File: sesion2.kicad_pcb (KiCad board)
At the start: 2 copper layers, 45 x 35.5 mm, 14 parts, among them IC1 AT89LS51-16AU, J1 1366004, J2 68000-106HLF

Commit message: Sesion4
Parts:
- removed PS1: TAR5SB30_TE85L,F_, Samacsys:SOT95P275X140-5N
- added C8: 100 nF, Capacitor_SMD:C_0402_1005Metric, F.Cu at (94.1, 100.0)
- added C9: 100nF, Capacitor_SMD:C_0402_1005Metric, F.Cu at (92.5, 122.0)
- added CCOMP1: 82 nF, Capacitor_SMD:C_0402_1005Metric, F.Cu at (82.5, 120.4)
- added CCOMP2: 180pF, Capacitor_SMD:C_0402_1005Metric, F.Cu at (77.4, 120.4)
- added Cboot1: 100 nF, Capacitor_SMD:C_0402_1005Metric, F.Cu at (81.5, 115.0)
- added Cin1: 4.7 uF, Capacitor_SMD:C_0402_1005Metric, F.Cu at (78.0, 110.5)
- added Cin2: 4.7 uF, Capacitor_SMD:C_0402_1005Metric, F.Cu at (80.0, 110.5)
- added Cout1: 22 uF, Capacitor_SMD:C_0402_1005Metric, F.Cu at (97.0, 111.0)
- added Cout2: 22 uF, Capacitor_SMD:C_0402_1005Metric, F.Cu at (95.0, 111.0)
- added D1: B560C, Samacsys:DIOM7959X250N, F.Cu at (90.5, 114.0)
- added IC2: VL53L1CXV0FY_1, Samacsys:VL53L1CXV0FY1, F.Cu at (97.3, 97.4)
- added IC3: MAX31855SASA+T, Samacsys:SOIC127P600X175-8N, F.Cu at (123.0, 100.0)
- added IC4: DS18B20Z+, Package_SO:SOIC-8_3.9x4.9mm_P1.27mm, F.Cu at (97.5, 128.0)
- added J3: Conn_01x05, Connector_PinHeader_2.54mm:PinHeader_1x05_P2.54mm_Vertical, F.Cu at (105.1, 135.0)
- added J4: Conn_01x02, TerminalBlock_Altech:Altech_AK100_1x02_P5.00mm, F.Cu at (126.0, 115.5)
- added J5: USB_C_Receptacle_USB2.0_16P, Connector_USB:USB_C_Receptacle_GCT_USB4105-xx-A_16P_TopMnt_Horizontal, F.Cu at (77.5, 131.5)
- added L1: 10uH, Inductor_SMD:L_1206_3216Metric, F.Cu at (96.0, 116.0)
- added R10: 5.1k, Resistor_SMD:R_0402_1005Metric_Pad0.72x0.64mm_HandSolder, F.Cu at (85.0, 134.5)
- added R4: 10k, Resistor_SMD:R_0402_1005Metric_Pad0.72x0.64mm_HandSolder, F.Cu at (110.5, 132.0)
- added R5: 4.7k, Resistor_SMD:R_0402_1005Metric_Pad0.72x0.64mm_HandSolder, F.Cu at (103.5, 124.5)
- added R6: 3.3k, Resistor_SMD:R_0402_1005Metric_Pad0.72x0.64mm_HandSolder, F.Cu at (103.0, 115.6)
- added R7: 3.3k, Resistor_SMD:R_0402_1005Metric_Pad0.72x0.64mm_HandSolder, F.Cu at (100.5, 96.0)
- added R8: 3.3k, Resistor_SMD:R_0402_1005Metric_Pad0.72x0.64mm_HandSolder, F.Cu at (110.0, 94.0)
- added R9: 5.1k, Resistor_SMD:R_0402_1005Metric_Pad0.72x0.64mm_HandSolder, F.Cu at (88.4, 134.5)
- added RCOMP1: 3.24, Resistor_SMD:R_0402_1005Metric_Pad0.72x0.64mm_HandSolder, F.Cu at (80.0, 120.4)
- added REN1: 100k, Resistor_SMD:R_0402_1005Metric_Pad0.72x0.64mm_HandSolder, F.Cu at (77.1, 106.5)
- added REN2: 10k, Resistor_SMD:R_0402_1005Metric_Pad0.72x0.64mm_HandSolder, F.Cu at (80.0, 106.5)
- added RFB1: 31.2k, Resistor_SMD:R_0402_1005Metric_Pad0.72x0.64mm_HandSolder, F.Cu at (74.4, 123.0)
- added RFB2: 10k, Resistor_SMD:R_0402_1005Metric_Pad0.72x0.64mm_HandSolder, F.Cu at (77.9, 123.0)
- added RRT1: 340k, Resistor_SMD:R_0402_1005Metric_Pad0.72x0.64mm_HandSolder, F.Cu at (74.0, 115.0)
- added U1: TPS54360BDDA, Samacsys:SOIC127P600X170-9N, F.Cu at (78.0, 115.0)
- added U2: CH340C, Package_SO:SOIC-16_3.9x9.9mm_P1.27mm, F.Cu at (88.0, 126.7)
- C1: value 1uF -> 100nF
- C2: value 0.01uF -> 100nF
- C3: value 10uF -> 100nF
- C5: value 100nF -> 10 nF
- C6: value 100nF -> 100 nF
- C7: value 100nF -> 4.7 nF
- IC1: value AT89LS51-16AU -> PIC16F18855-I_SP; footprint Samacsys:QFP80P1200X1200X120-44N -> Samacsys:DIP794W56P254L3486H508Q28N
- J1: value 1366004 -> TB0012-508-02GR; footprint Samacsys:1366004 -> Samacsys:TB0012-508-02GR
- J2: value 68000-106HLF -> Conn_01x05; footprint Samacsys:HDRV6W64P0X254_1X6_1524X254X839P -> Connector_PinHeader_2.54mm:PinHeader_1x05_P2.54mm_Vertical
- R1, R2, R3: value 10k -> 1k
- moved C7 63.1 mm to (94.1, 98.0), turned to -90 degrees
- moved C6 62.6 mm to (102.5, 127.4)
- moved J1 58.4 mm to (76.5, 98.0)
- moved R3 50.7 mm to (120.5, 131.5), turned to 90 degrees
- moved C4 48.6 mm to (104.5, 110.0), turned to -90 degrees
- moved R2 46.4 mm to (123.0, 131.5), turned to 90 degrees
- moved J2 45.1 mm to (128.1, 135.0), turned to -90 degrees
- moved IC1 42.7 mm to (110.5, 113.0), turned to 180 degrees
- moved R1 41.8 mm to (125.5, 131.5), turned to 90 degrees
- moved C3 38.9 mm to (120.5, 128.5), turned to 0 degrees
- moved C1 34.3 mm to (125.5, 128.5), turned to 0 degrees
- moved C2 32.7 mm to (123.0, 128.5), turned to 0 degrees
- moved C5 28.1 mm to (128.8, 100.1), turned to 90 degrees
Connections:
- C1 pad 1: +9V -> Net-(IC1-RA2)
- C2 pad 1: Net-(PS1-NOISE) -> Net-(IC1-RA1)
- C3 pad 1: /Alimentacion/Vout3v -> Net-(IC1-RA0)
- C4 pad 1: Net-(IC1-P1.2) -> /Alimentacion/3.3v
- C5 pad 1: Net-(IC1-P1.1) -> Net-(IC3-T-)
- C5 pad 2: GND -> Net-(IC3-T+)
- C6 pad 1: Net-(IC1-P1.0) -> /Alimentacion/3.3v
- C7 pad 1: /Alimentacion/Vout3v -> GND
- C7 pad 2: GND -> /Alimentacion/3.3v
- IC1 pad 1: unconnected-(IC1-(MOSI)_P1.5-Pad1) -> /Microcontrolador/MCLR/VPP
- IC1 pad 11: unconnected-(IC1-(T1)_P3.5-Pad11) -> /Microcontrolador/SPI_SCK
- IC1 pad 12: unconnected-(IC1-(~{WR)_P3.6}-Pad12) -> /Microcontrolador/SPI_MISO
- IC1 pad 13: unconnected-(IC1-(~{RD)_P3.7}-Pad13) -> /Microcontrolador/SPI_CS
- IC1 pad 14: unconnected-(IC1-XTAL2-Pad14) -> /Microcontrolador/I2C_SCL
- IC1 pad 15: unconnected-(IC1-XTAL1-Pad15) -> /Microcontrolador/I2C_SDA
- IC1 pad 16: GND -> unconnected-(IC1-RC5-Pad16)
- IC1 pad 17: unconnected-(IC1-GND_2-Pad17) -> /Microcontrolador/UART_TX
- IC1 pad 18: unconnected-(IC1-(A8)_P2.0-Pad18) -> /Microcontrolador/UART_RX
- IC1 pad 19: unconnected-(IC1-(A9)_P2.1-Pad19) -> GND
- IC1 pad 2: unconnected-(IC1-(MISO)_P1.6-Pad2) -> Net-(IC1-RA0)
- IC1 pad 20: unconnected-(IC1-(A10)_P2.2-Pad20) -> /Alimentacion/3.3v
- IC1 pad 25: unconnected-(IC1-P2.7_(A15)-Pad25) -> /Microcontrolador/XHUT
- IC1 pad 26: unconnected-(IC1-~{PSEN}-Pad26) -> /Microcontrolador/DQ
- IC1 pad 27: unconnected-(IC1-ALE/~{PROG}-Pad27) -> /Microcontrolador/PGC
- IC1 pad 28: unconnected-(IC1-NC_2-Pad28) -> /Microcontrolador/PGD
- IC1 pad 3: unconnected-(IC1-(SCK)_P1.7-Pad3) -> Net-(IC1-RA1)
- IC1 pad 4: unconnected-(IC1-RST-Pad4) -> Net-(IC1-RA2)
- IC1 pad 8: unconnected-(IC1-(~{INT0)_P3.2}-Pad8) -> GND
- J1 pad 1: +9V -> Net-(U1-VIN)
- J2 pad 1: /Alimentacion/Vout3v -> GND
- J2 pad 2: GND -> Net-(J2-Pin_2)
- J2 pad 3: Net-(J2-Pad3) -> Net-(J2-Pin_3)
- J2 pad 4: Net-(J2-Pad4) -> Net-(J2-Pin_4)
- J2 pad 5: Net-(J2-Pad5) -> /Alimentacion/3.3v
- R1 pad 1: Net-(J2-Pad3) -> Net-(J2-Pin_2)
- R1 pad 2: Net-(IC1-P1.2) -> Net-(IC1-RA2)
- R2 pad 1: Net-(J2-Pad4) -> Net-(J2-Pin_3)
- R2 pad 2: Net-(IC1-P1.1) -> Net-(IC1-RA1)
- R3 pad 1: Net-(J2-Pad5) -> Net-(J2-Pin_4)
- R3 pad 2: Net-(IC1-P1.0) -> Net-(IC1-RA0)
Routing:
- net /Alimentacion/Vout3v: track 53.3 -> 0.00 mm
- net /Microcontrolador/UART_TX: track 0.00 -> 45.3 mm, vias 0 -> 1
- net /Microcontrolador/UART_RX: track 0.00 -> 44.2 mm, vias 0 -> 1
- net /Microcontrolador/XHUT: track 0.00 -> 37.4 mm
- net /Alimentacion/3.3v: track 0.00 -> 34.7 mm, vias 0 -> 11
- net GND: track 8.54 -> 34.7 mm, vias 9 -> 25
- net Net-(IC3-T+): track 0.00 -> 22.1 mm
- net /Microcontrolador/I2C_SCL: track 0.00 -> 19.9 mm, vias 0 -> 2
- net Net-(D1-K): track 0.00 -> 18.2 mm
- net Net-(U1-VIN): track 0.00 -> 18.1 mm, vias 0 -> 2
- net +9V: track 17.7 -> 0.00 mm
- net /Microcontrolador/PGD: track 0.00 -> 17.3 mm
- net Net-(IC1-P1.0): track 15.9 -> 0.00 mm
- net Net-(IC1-RA2): track 0.00 -> 15.8 mm
- net /Microcontrolador/SPI_MISO: track 0.00 -> 14.8 mm
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- added copper zone on In2.Cu, net /Alimentacion/3.3v
- added copper zone on In1.Cu, net GND
- removed copper zone on B.Cu, net GND
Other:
- board size 45 x 35.5 mm -> 58 x 45.5 mm
- copper layers 2 -> 4

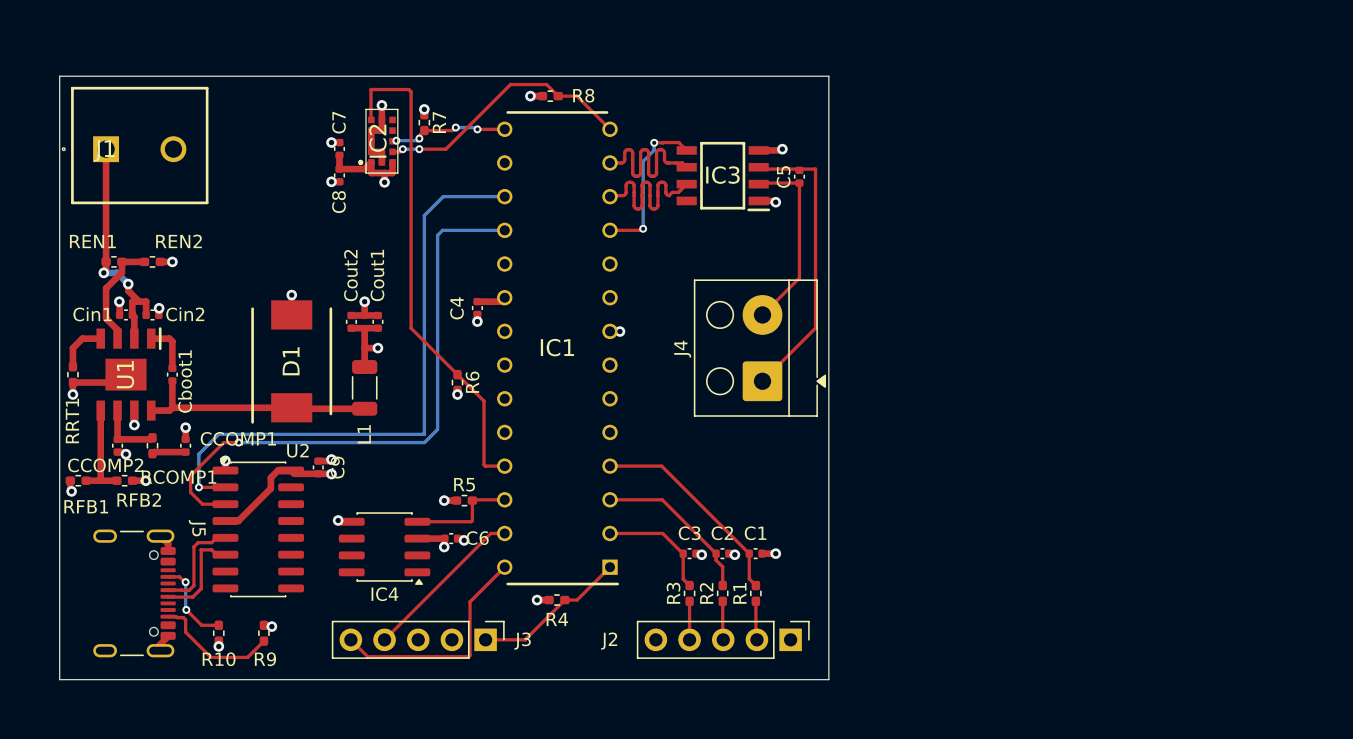
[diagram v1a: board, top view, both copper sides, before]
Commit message: Se han solucionado los errores de DRC, se ha actualizado la pcb y se han añadido vias de borde y de transición
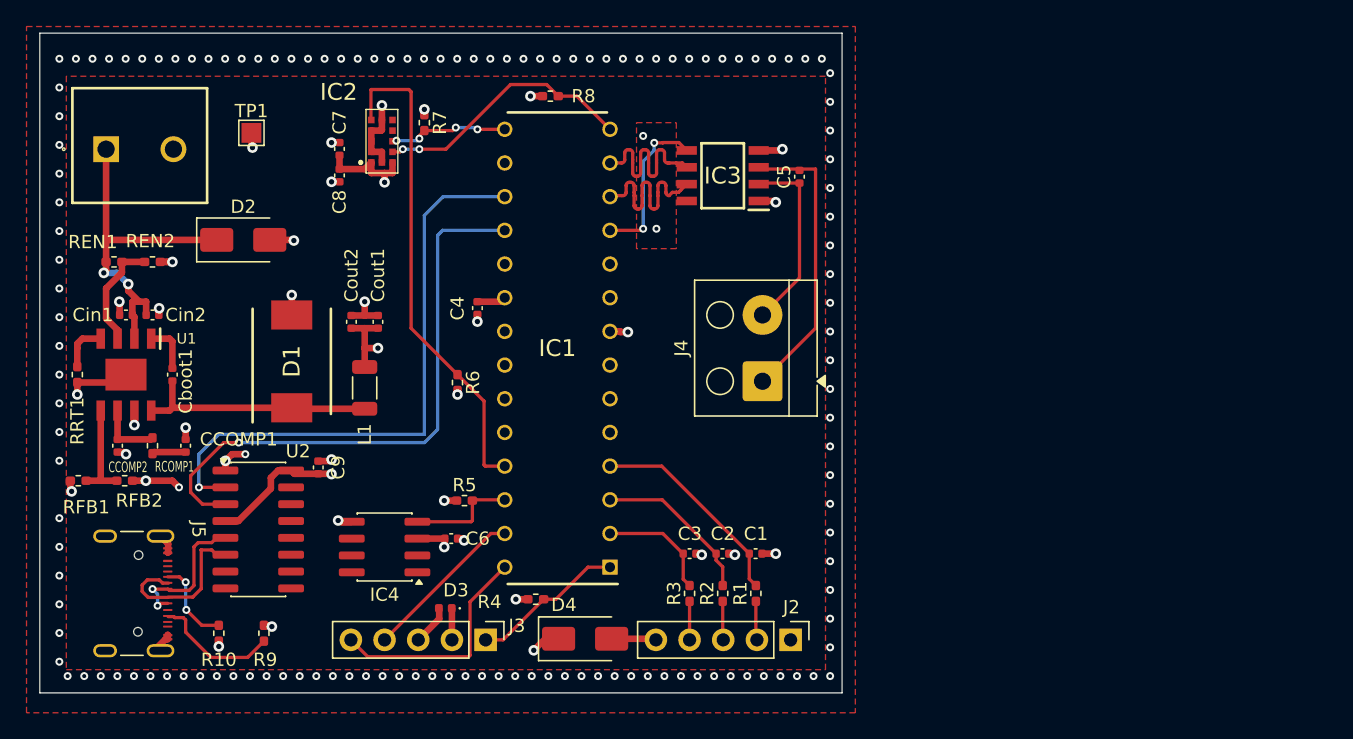
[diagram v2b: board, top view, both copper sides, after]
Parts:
- added D2: D_TVS, Diode_SMD:D_SMA, F.Cu at (86.8, 104.8)
- added D3: D_TVS, Diode_SMD:D_0402_1005Metric, F.Cu at (102.1, 132.6)
- added D4: D_TVS, Diode_SMD:D_SMA, F.Cu at (112.6, 134.9)
- added TP1: TestPoint, TestPoint:TestPoint_Pad_1.5x1.5mm, F.Cu at (87.5, 96.8)
- moved R4 1.60 mm to (108.9, 131.9)
- moved RRT1 0.33 mm to (74.3, 115.0)
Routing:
- net GND: track 34.7 -> 48.3 mm, vias 25 -> 166
- net Net-(D2-A1): track 18.1 -> 26.6 mm
- net /Alimentacion/3.3v: track 34.7 -> 41.6 mm, vias 11 -> 12
- net /Microcontrolador/USB_D-: track 7.72 -> 12.5 mm
- net /Microcontrolador/USB_D+: track 7.72 -> 11.1 mm, vias 0 -> 2
- added copper zone on F.Cu, net GND
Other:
- board size 58 x 45.5 mm -> 60.5 x 49.8 mm
